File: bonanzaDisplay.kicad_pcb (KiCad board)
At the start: 6 copper layers, 27.9 x 89.5 mm, 78 parts, among them J1 OLED-1.31-SSD1322, J15 SWD, J2 Conn_01x02, J5 Conn_01x10, J6 TYPE-C-31-M-12, SW1 TS-1088-AR02016, SW2 TS-1088-AR02016, SW3 SIQ-02FVS3, U1 RP2354A, U2 XC6206P302MR, U3 XC6206P282MR, U4 TPS62933DRLR, Y1 ABM8-272-T3

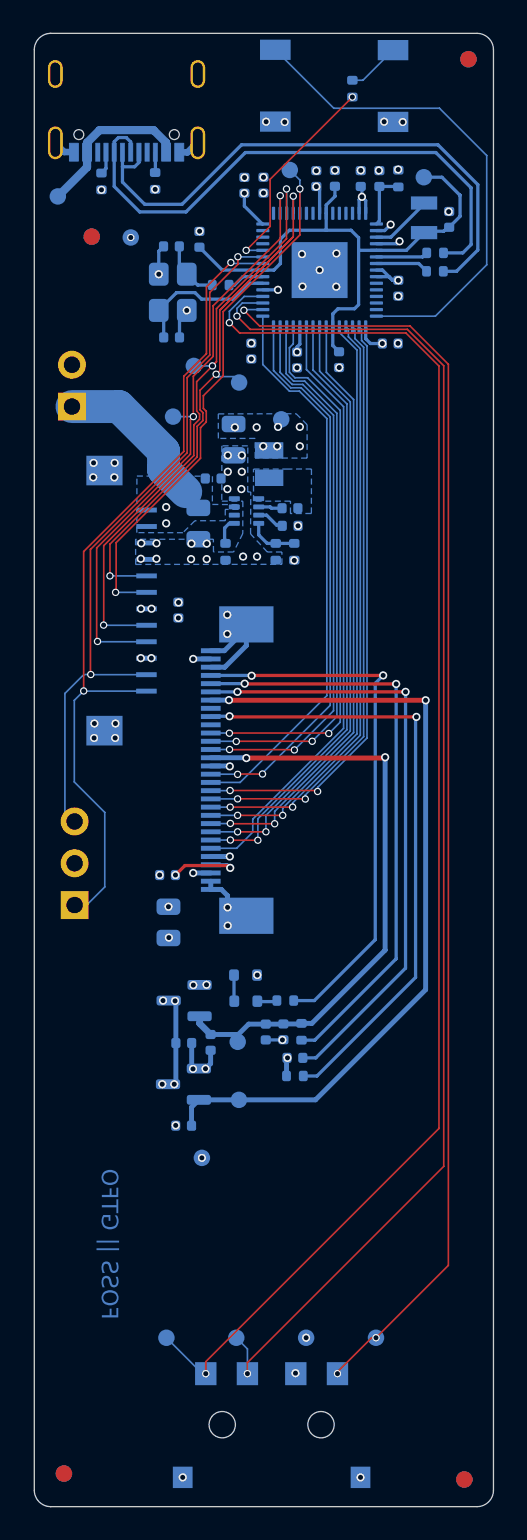
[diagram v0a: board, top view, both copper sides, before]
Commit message: removed the OLED accessory voltage regulators -- we should be good with 3.3V. addressed VCOMH bypass cap voltage rating.
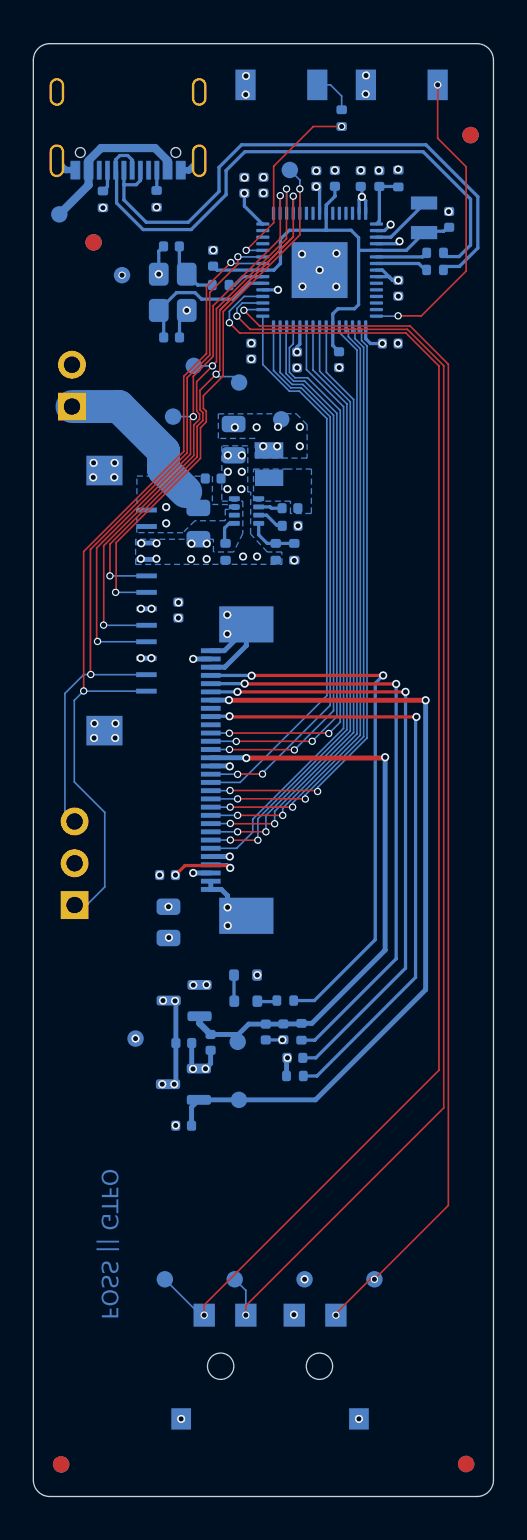
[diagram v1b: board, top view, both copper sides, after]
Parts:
- removed TP17: 1V1, bonanzaDisplay:TestPoint_Pad_D1.0mm
- moved TP18 8.29 mm to (129.4, 105.8)
- moved SW2 7.68 mm to (145.6, 47.9), turned to 180 degrees
- moved SW1 6.78 mm to (138.3, 47.9), turned to 180 degrees
- moved FID2 4.61 mm to (149.8, 50.9)
- moved SW3 3.55 mm to (137.6, 125.8)
- moved TP12 3.55 mm to (131.2, 120.4)
- moved TP13 3.55 mm to (135.4, 120.4)
- moved TP14 3.55 mm to (143.9, 120.4)
- moved TP24 3.55 mm to (139.7, 120.4)
- moved TP19 2.35 mm to (128.6, 59.4)
- moved R33 1.90 mm to (141.9, 49.9)
- moved C20 1.42 mm to (134.1, 58.4)
- moved R2 1.09 mm to (127.4, 54.8)
- moved J6 1.09 mm to (128.9, 49.3)
- moved R4 1.09 mm to (130.7, 54.8)
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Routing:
- net Net-(U1-~{QSPI_SS}): track 30.1 -> 18.6 mm, vias 0 -> 2
- net /1V1: track 34.5 -> 28.3 mm
- net /SW_SW: track 84.6 -> 81.1 mm
- net /SW_CCW: track 87.3 -> 83.8 mm
- net /SW_CW: track 79.2 -> 75.7 mm
- net Net-(U1-RUN): track 12.9 -> 11.9 mm
- net /USB_DN: track 34.6 -> 35.5 mm
- net /USB_DP: track 35.0 -> 35.8 mm
- net Net-(R33-Pad2): track 3.23 -> 2.59 mm
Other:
- board size 27.9 x 89.5 mm -> 27.9 x 88.2 mm

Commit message: Sync reviewed v3.1 PCB fixes and protect BOOT chip-select
Add R40 (1k, 0402, C11702) between QSPI_SS and SW2, including the
reviewed via placement on its switch-side pad and refreshed zone fills.

Include the manually synchronized OLED power, bypass capacitor and
crystal changes, corrected C16/C17 MPNs, connector datasheet links,
and the v3.1 project revision metadata.

Validation: zero DRC violations, zero unconnected items, and zero
schematic/PCB parity mismatches. All 19 existing ERC findings are
unchanged. Hardware BOOTSEL testing and assembly-process checks remain
open.

Refs #3, #4, #5, #6, #8, #9, #12, #16
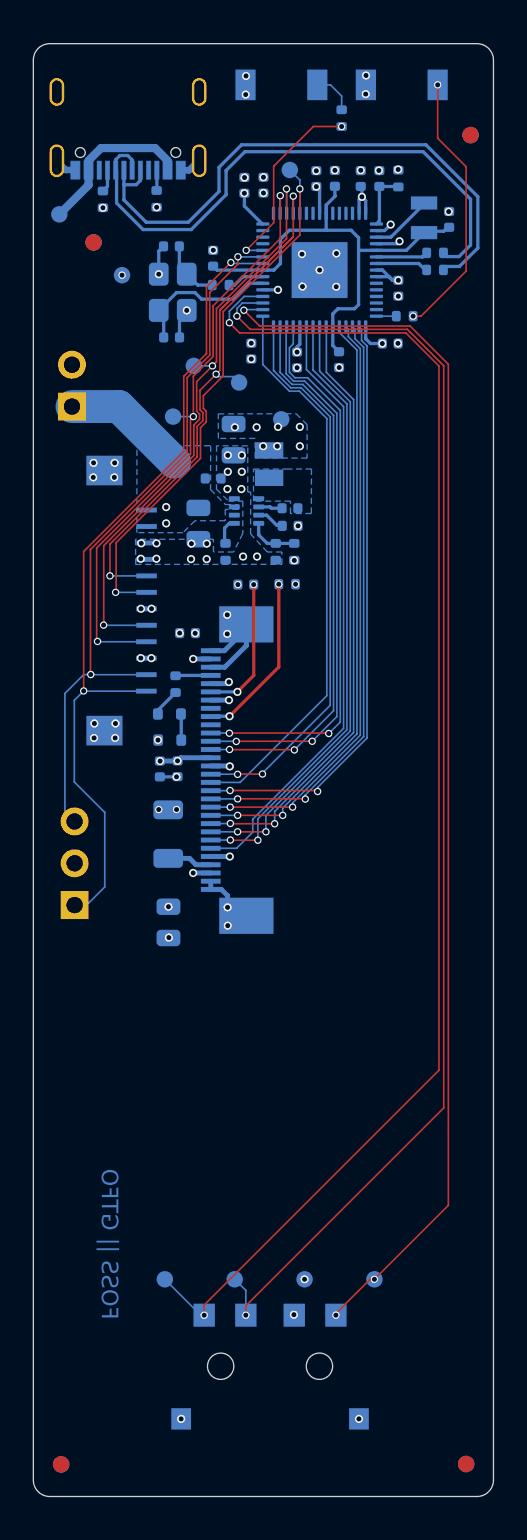
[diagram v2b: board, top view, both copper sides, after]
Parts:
- removed C38, C39, C40: 1uF, Capacitor_SMD:C_0402_1005Metric
- removed R39: 4.7k, Resistor_SMD:R_0402_1005Metric
- removed TP15: 3V0, bonanzaDisplay:TestPoint_Pad_D1.0mm
- removed TP16: 2V8, bonanzaDisplay:TestPoint_Pad_D1.0mm
- removed TP18: GND, bonanzaDisplay:TestPoint_Pad_D1.0mm
- removed U2: XC6206P302MR, Package_TO_SOT_SMD:SOT-23
- removed U3: XC6206P282MR, Package_TO_SOT_SMD:SOT-23
- added R40: 1k, Resistor_SMD:R_0402_1005Metric, B.Cu at (145.8, 61.9)
- C16, C17: value 10pF -> 15pF
- C26: footprint Capacitor_SMD:C_0402_1005Metric -> Capacitor_SMD:C_1206_3216Metric
- J1: value OLED-1.31-SSD1322 -> OLED-3.12-SSD1322
- J5: value Conn_01x10 -> Conn_01x12
- moved R35 29.9 mm to (138.6, 78.2), turned to 0 degrees
- moved C22 28.9 mm to (136.1, 78.2)
- moved R34 20.3 mm to (131.8, 84.3), turned to 90 degrees
- moved D3 18.1 mm to (131.5, 86.1), turned to 180 degrees
- moved C19 17.2 mm to (131.9, 89.4)
- moved C21 17.2 mm to (130.9, 89.4)
- moved D2 15.0 mm to (131.5, 87.7), turned to 0 degrees
- moved C26 2.49 mm to (131.4, 93.4), turned to 90 degrees
- moved C35 1.51 mm to (132.6, 81.2), turned to 0 degrees
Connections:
- C19 pad 1: /3V0 -> /3V3
- C21 pad 1: /3V0 -> /3V3
- J1 pad 17: /3V0 -> /3V3
- J1 pad 24: /2V8 -> /3V3
- J1 pad 26: Net-(J1-VCI) -> /3V3
- SW2 pad 1: Net-(U1-~{QSPI_SS}) -> Net-(R40-Pad2)
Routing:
- net /2V8: track 49.2 -> 0.00 mm, vias 2 -> 0
- net /3V0: track 36.5 -> 0.00 mm, vias 2 -> 0
- net Net-(J1-VCI): track 35.8 -> 0.00 mm, vias 2 -> 0
- net Net-(J1-VSL): track 33.2 -> 2.26 mm, vias 2 -> 0
- net Net-(J1-VDD): track 37.1 -> 8.55 mm
- net Net-(J1-IREF): track 37.7 -> 10.4 mm
- net Net-(U1-~{QSPI_SS}): track 18.6 -> 1.21 mm, vias 2 -> 0
- net Net-(R40-Pad2): track 0.00 -> 16.4 mm, vias 0 -> 2
- net /GND: track 25.1 -> 21.1 mm, vias 79 -> 75
- net /12V: track 38.6 -> 35.4 mm
- net Net-(J1-VCOMH): track 4.88 -> 2.75 mm, vias 2 -> 0
- net Net-(D3-A): track 1.37 -> 1.92 mm
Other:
- board text added: "bonanzaDisplay v3.1"
- board text removed: "bonanzaDisplay v3"

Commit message: Apply reviewed fabrication rules and ERC model fixes
Configure JLCPCB six-layer DFM rules and correct via drills, USB VBUS clearances, and silkscreen. Document filled-and-capped via requirements and remaining supplier preview checks.

Correct project symbol pin types and add verified power-source assertions without changing circuit connectivity. ERC, DRC, unconnected-item and schematic parity checks pass.

Refs #11, #12, #15
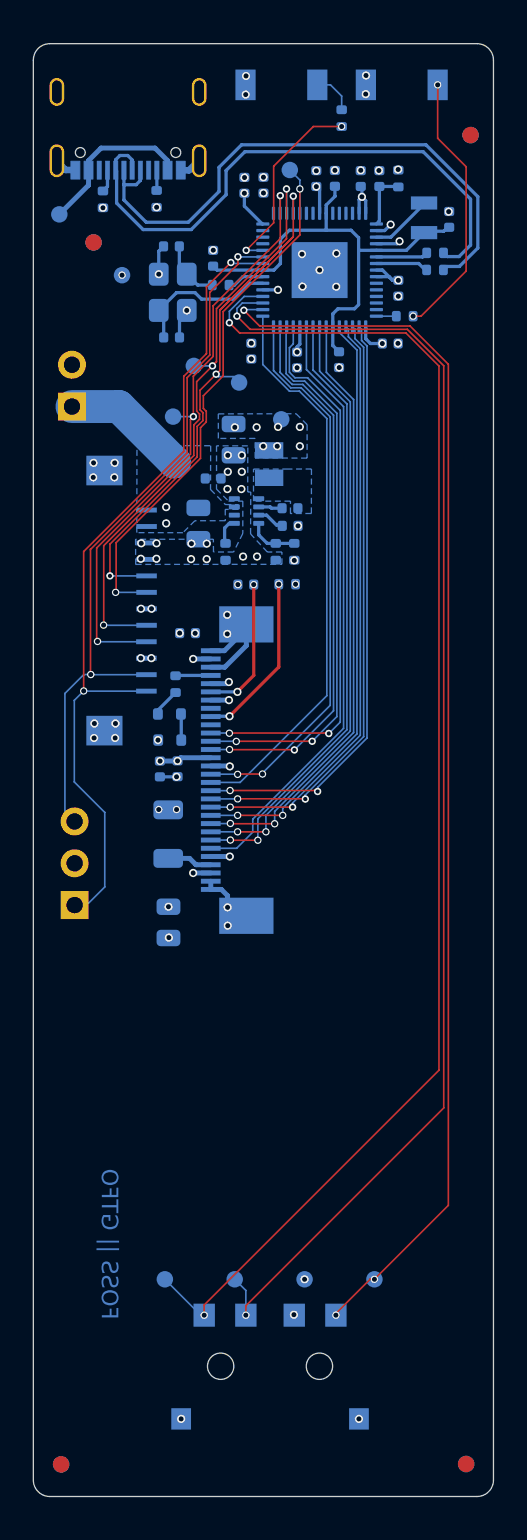
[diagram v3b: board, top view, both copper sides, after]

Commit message: Add encoder pull-ups and document bonanzaDisplay v3.1
Add three 4.7k pull-ups using JLCPCB Basic part C25900 and route them on the PCB. Expand the README with hardware, interface, development, and manufacturing information.

Validation: ERC, DRC, unconnected-item checks, and schematic/PCB parity all pass.
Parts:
- added R41: 4.7k, Resistor_SMD:R_0402_1005Metric, B.Cu at (145.6, 114.7)
- added R42: 4.7k, Resistor_SMD:R_0402_1005Metric, B.Cu at (142.9, 114.7)
- added R43: 4.7k, Resistor_SMD:R_0402_1005Metric, B.Cu at (140.3, 114.7)
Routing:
- net /SW_SW: vias 2 -> 3
- net /SW_CW: vias 3 -> 4
- net /SW_CCW: vias 2 -> 3
- net /3V3: vias 23 -> 26

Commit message: Correct OLED IREF resistor and reconcile BOM ratings
Set R35 to 750k and synchronize manufacturer, MPN, and actual passive ratings across the schematic and PCB. Document DC-bias and inductor qualification concerns and update manufacturing guidance.
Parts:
- R35: value 590k -> 750k
